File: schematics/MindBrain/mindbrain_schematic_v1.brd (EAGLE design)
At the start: 100 x 80 mm, 47 parts, among them CON1 POWER, IC1 TL084P, IC2 TL084P

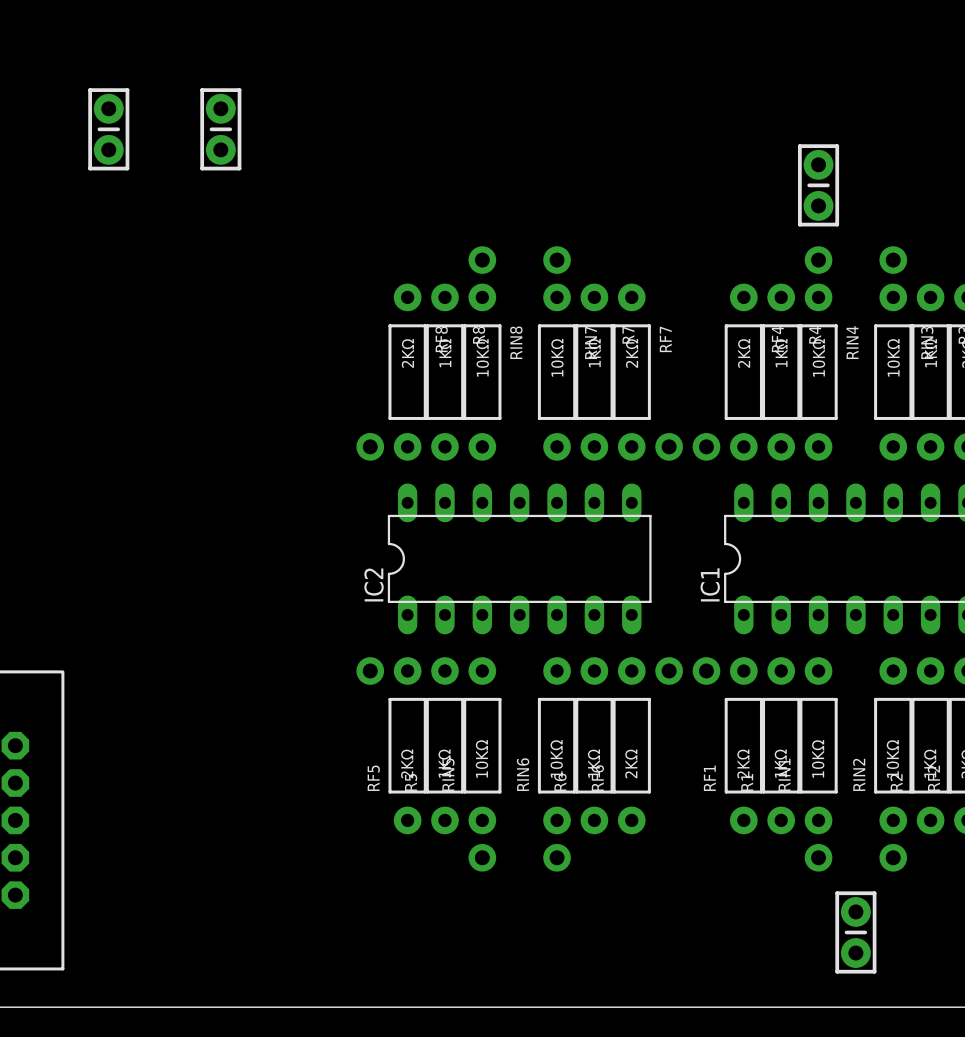
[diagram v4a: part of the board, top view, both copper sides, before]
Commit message: placed bypass caps in board view
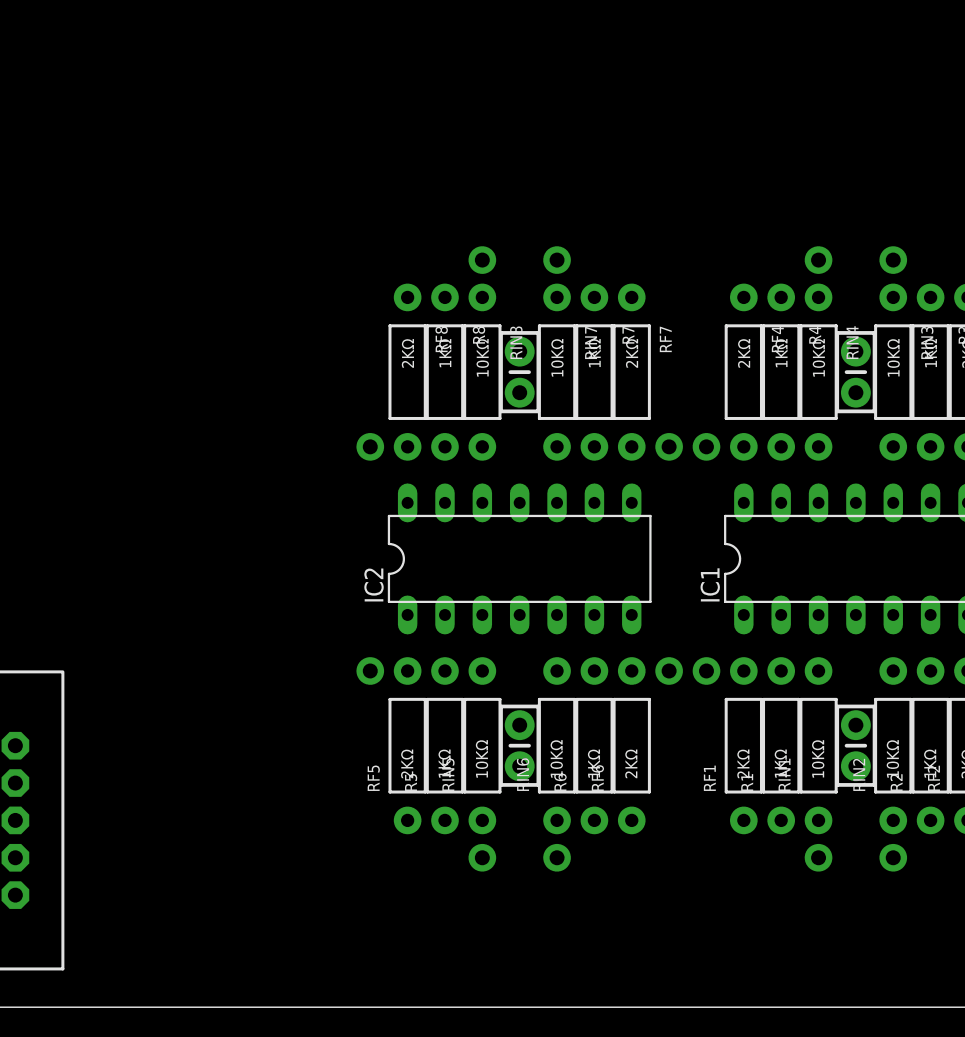
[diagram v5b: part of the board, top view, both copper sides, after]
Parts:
- moved C1 50.4 mm to (41.9, 17.8), turned to 270 degrees
- moved C3 38.2 mm to (64.8, 17.8), turned to 270 degrees
- moved C2 38.1 mm to (64.8, 43.2)
- moved C4 26.2 mm to (41.9, 43.2)
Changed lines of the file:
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@@
 <element name="RIN7" library="SparkFun-Passives" package="AXIAL-0.4" value="10KΩ" x="44.45" y="43.18" rot="R270"/>
 <element name="RIN8" library="SparkFun-Passives" package="AXIAL-0.4" value="10KΩ" x="39.37" y="43.18" rot="R270"/>
-<element name="C1" library="SparkFun-Capacitors" package="CAP-PTH-SMALL-KIT" value="0.1uF" x="13.97" y="59.69" rot="R90"/>
-<element name="C2" library="SparkFun-Capacitors" package="CAP-PTH-SMALL-KIT" value="0.1uF" x="64.77" y="5.08" rot="R90"/>
-<element name="C3" library="SparkFun-Capacitors" package="CAP-PTH-SMALL-KIT" value="0.1uF" x="62.23" y="55.88" rot="R90"/>
-<element name="C4" library="SparkFun-Capacitors" package="CAP-PTH-SMALL-KIT" value="0.1uF" x="21.59" y="59.69" rot="R90"/>
+<element name="C1" library="SparkFun-Capacitors" package="CAP-PTH-SMALL-KIT" value="0.1uF" x="41.91" y="17.78" rot="R270"/>
+<element name="C2" library="SparkFun-Capacitors" package="CAP-PTH-SMALL-KIT" value="0.1uF" x="64.77" y="43.18" rot="R90"/>
+<element name="C3" library="SparkFun-Capacitors" package="CAP-PTH-SMALL-KIT" value="0.1uF" x="64.77" y="17.78" rot="R270"/>
+<element name="C4" library="SparkFun-Capacitors" package="CAP-PTH-SMALL-KIT" value="0.1uF" x="41.91" y="43.18" rot="R90"/>
 <element name="CON1" library="SparkFun-Connectors" package="2X5-SHROUDED" value="POWER" x="6.35" y="12.7"/>
 </elements>
@@
 <wire x1="62.23" y1="48.26" x2="67.31" y2="48.26" width="0" layer="19" extent="1-1"/>
 <wire x1="59.69" y1="48.26" x2="62.23" y2="48.26" width="0" layer="19" extent="1-1"/>
-<wire x1="62.23" y1="57.277" x2="62.23" y2="48.26" width="0" layer="19" extent="1-1"/>
+<wire x1="64.77" y1="16.383" x2="62.23" y2="48.26" width="0" layer="19" extent="1-1"/>
 <wire x1="46.99" y1="48.26" x2="59.69" y2="48.26" width="0" layer="19" extent="1-1"/>
 <wire x1="44.45" y1="48.26" x2="46.99" y2="48.26" width="0" layer="19" extent="1-1"/>
 <wire x1="39.37" y1="48.26" x2="44.45" y2="48.26" width="0" layer="19" extent="1-1"/>
 <wire x1="36.83" y1="48.26" x2="39.37" y2="48.26" width="0" layer="19" extent="1-1"/>
-<wire x1="21.59" y1="61.087" x2="36.83" y2="48.26" width="0" layer="19" extent="1-1"/>
-<wire x1="13.97" y1="61.087" x2="21.59" y2="61.087" width="0" layer="19" extent="1-1"/>
+<wire x1="41.91" y1="44.577" x2="36.83" y2="48.26" width="0" layer="19" extent="1-1"/>
+<wire x1="41.91" y1="16.383" x2="41.91" y2="44.577" width="0" layer="19" extent="1-1"/>
 <wire x1="69.85" y1="12.7" x2="69.85" y2="48.26" width="0" layer="19" extent="1-1"/>
 <wire x1="67.31" y1="12.7" x2="69.85" y2="12.7" width="0" layer="19" extent="1-1"/>
 <wire x1="62.23" y1="12.7" x2="67.31" y2="12.7" width="0" layer="19" extent="1-1"/>
 <wire x1="59.69" y1="12.7" x2="62.23" y2="12.7" width="0" layer="19" extent="1-1"/>
-<wire x1="64.77" y1="6.477" x2="67.31" y2="12.7" width="0" layer="19" extent="1-1"/>
+<wire x1="64.77" y1="44.577" x2="67.31" y2="12.7" width="0" layer="19" extent="1-1"/>
 <wire x1="46.99" y1="12.7" x2="59.69" y2="12.7" width="0" layer="19" extent="1-1"/>
 <wire x1="44.45" y1="12.7" x2="46.99" y2="12.7" width="0" layer="19" extent="1-1"/>
@@
 <contactref element="C4" pad="1"/>
 <wire x1="41.91" y1="34.29" x2="64.77" y2="34.29" width="0" layer="19" extent="1-1"/>
-<wire x1="64.77" y1="3.683" x2="64.77" y2="34.29" width="0" layer="19" extent="1-1"/>
-<wire x1="21.59" y1="58.293" x2="41.91" y2="34.29" width="0" layer="19" extent="1-1"/>
+<wire x1="64.77" y1="41.783" x2="64.77" y2="34.29" width="0" layer="19" extent="1-1"/>
+<wire x1="41.91" y1="41.783" x2="41.91" y2="34.29" width="0" layer="19" extent="1-1"/>
 <wire x1="7.62" y1="17.78" x2="41.91" y2="34.29" width="0" layer="19" extent="1-1"/>
 <wire x1="5.08" y1="17.78" x2="7.62" y2="17.78" width="0" layer="19" extent="1-1"/>
@@
 <contactref element="C3" pad="1"/>
 <contactref element="CON1" pad="10"/>
-<wire x1="64.77" y1="26.67" x2="62.23" y2="54.483" width="0" layer="19" extent="1-1"/>
+<wire x1="64.77" y1="26.67" x2="64.77" y2="19.177" width="0" layer="19" extent="1-1"/>
 <wire x1="41.91" y1="26.67" x2="64.77" y2="26.67" width="0" layer="19" extent="1-1"/>
 <wire x1="7.62" y1="7.62" x2="41.91" y2="26.67" width="0" layer="19" extent="1-1"/>
 <wire x1="5.08" y1="7.62" x2="7.62" y2="7.62" width="0" layer="19" extent="1-1"/>
-<wire x1="13.97" y1="58.293" x2="41.91" y2="26.67" width="0" layer="19" extent="1-1"/>
+<wire x1="41.91" y1="19.177" x2="41.91" y2="26.67" width="0" layer="19" extent="1-1"/>
 </signal>
 </signals>

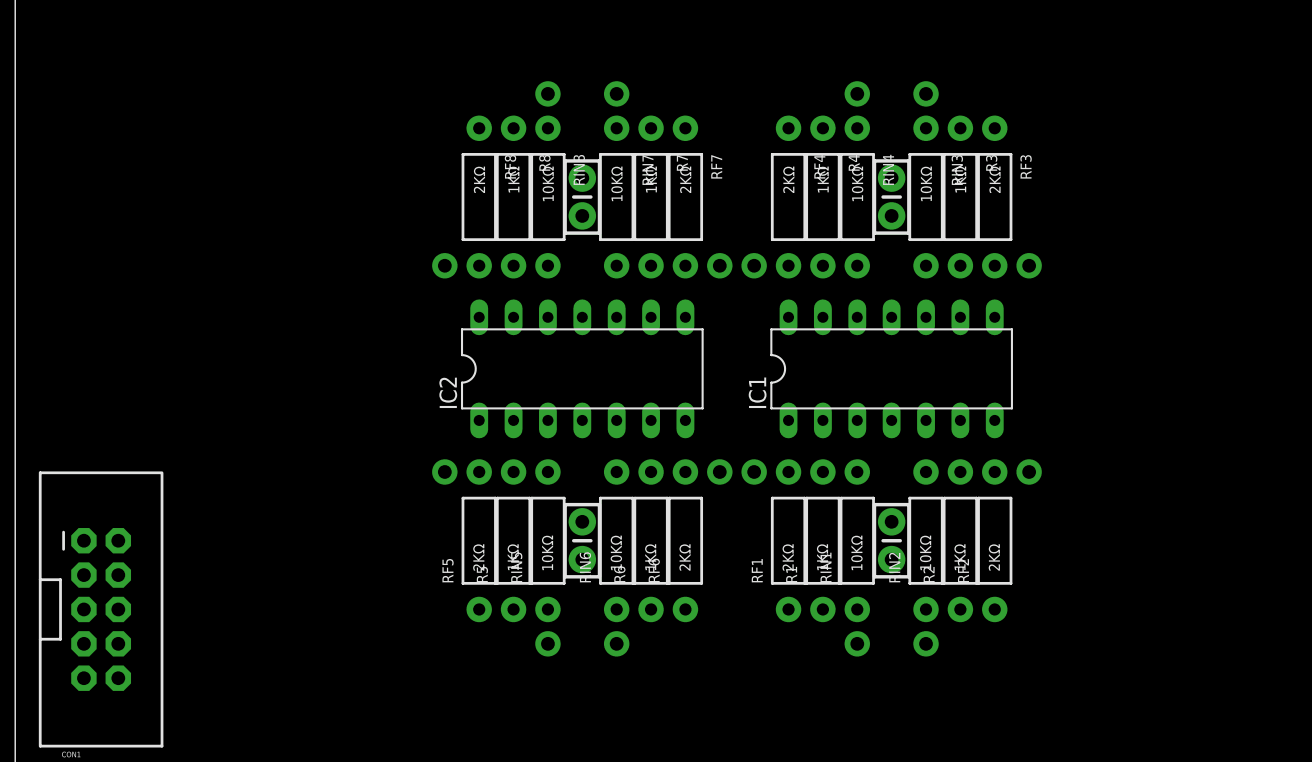
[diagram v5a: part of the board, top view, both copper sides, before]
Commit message: started laying traces, top side
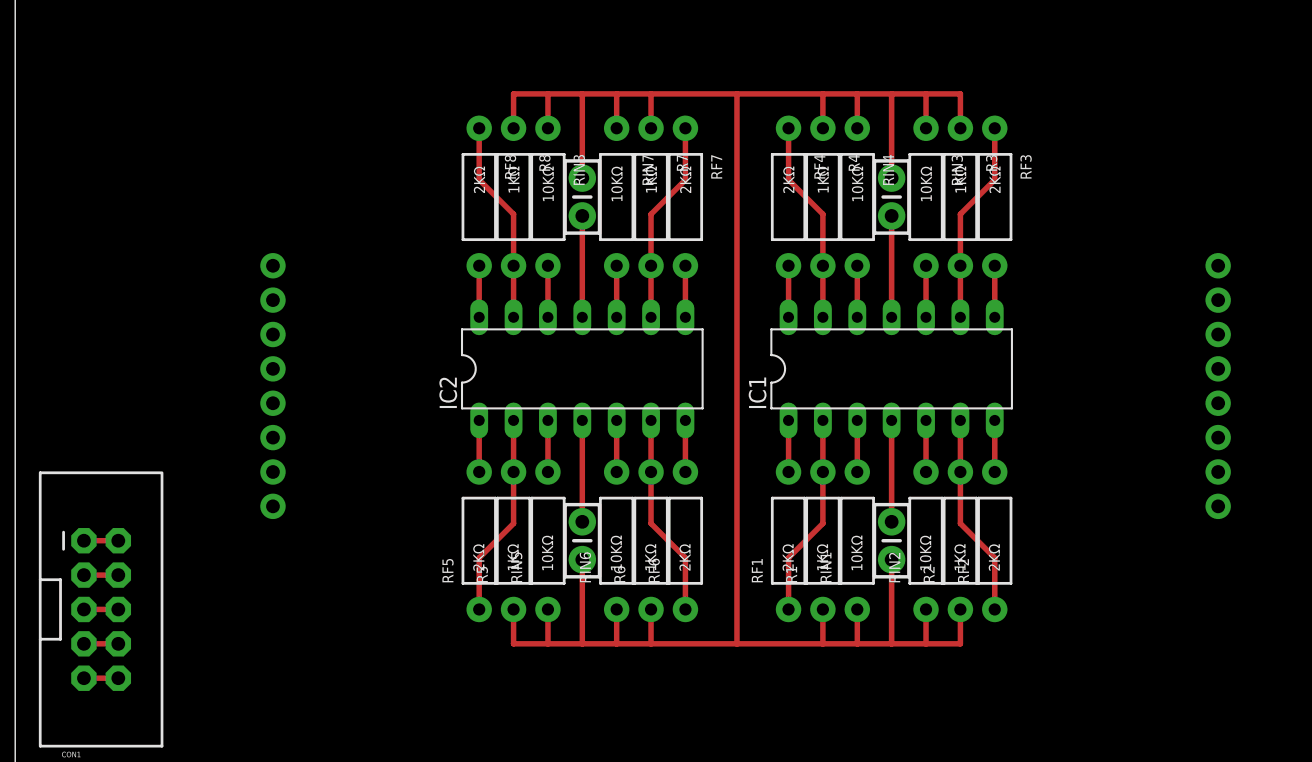
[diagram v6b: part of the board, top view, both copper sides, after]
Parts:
- moved OUTPUT5 57.7 mm to (88.9, 30.5)
- moved OUTPUT8 57.2 mm to (88.9, 38.1)
- moved INPUT3 54.5 mm to (19.1, 25.4)
- moved INPUT2 49.9 mm to (19.1, 22.9)
- moved INPUT4 48.9 mm to (19.1, 27.9)
- moved INPUT1 44.4 mm to (19.1, 20.3)
- moved OUTPUT6 38.2 mm to (88.9, 33.0)
- moved OUTPUT7 36.9 mm to (88.9, 35.6)
- moved OUTPUT4 35.8 mm to (88.9, 27.9)
- moved OUTPUT1 34.4 mm to (88.9, 20.3)
- moved INPUT6 34.2 mm to (19.1, 33.0)
- moved INPUT7 29.6 mm to (19.1, 35.6)
- moved INPUT5 28.7 mm to (19.1, 30.5)
- moved INPUT8 24.0 mm to (19.1, 38.1)
- moved OUTPUT3 18.9 mm to (88.9, 25.4)
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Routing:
- net GND: track 0.00 -> 179.8 mm
- net N$27: track 0.00 -> 17.5 mm
- net N$25: track 0.00 -> 17.5 mm
- net N$6: track 0.00 -> 15.0 mm
- net N$9: track 0.00 -> 15.0 mm
- net N$3: track 0.00 -> 15.0 mm
- net N$18: track 0.00 -> 15.0 mm
- net N$15: track 0.00 -> 15.0 mm
- net N$24: track 0.00 -> 15.0 mm
- net N$21: track 0.00 -> 15.0 mm
- net N$12: track 0.00 -> 15.0 mm
- net N$8: track 0.00 -> 3.81 mm
- net N$7: track 0.00 -> 3.81 mm
- net N$5: track 0.00 -> 3.81 mm
- net N$4: track 0.00 -> 3.81 mm
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
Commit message: updated top layer layouts
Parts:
- moved CON1 16.6 mm to (7.62, 29.2)
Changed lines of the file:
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@@
 <element name="C3" library="SparkFun-Capacitors" package="CAP-PTH-SMALL-KIT" value="0.1uF" x="64.77" y="17.78" rot="R270"/>
 <element name="C4" library="SparkFun-Capacitors" package="CAP-PTH-SMALL-KIT" value="0.1uF" x="41.91" y="43.18" rot="R90"/>
-<element name="CON1" library="SparkFun-Connectors" package="2X5-SHROUDED" value="POWER" x="6.35" y="12.7"/>
+<element name="CON1" library="SparkFun-Connectors" package="2X5-SHROUDED" value="POWER" x="7.62" y="29.21"/>
 </elements>
 <signals>
@@
 <contactref element="C1" pad="2"/>
 <contactref element="C3" pad="2"/>
-<wire x1="5.08" y1="10.16" x2="7.62" y2="10.16" width="0.4064" layer="1"/>
-<wire x1="5.08" y1="15.24" x2="7.62" y2="15.24" width="0.4064" layer="1"/>
-<wire x1="5.08" y1="12.7" x2="7.62" y2="12.7" width="0.4064" layer="1"/>
+<wire x1="6.35" y1="26.67" x2="8.89" y2="26.67" width="0.4064" layer="1"/>
+<wire x1="6.35" y1="31.75" x2="8.89" y2="31.75" width="0.4064" layer="1"/>
+<wire x1="6.35" y1="29.21" x2="8.89" y2="29.21" width="0.4064" layer="1"/>
 <wire x1="39.37" y1="12.7" x2="39.37" y2="10.16" width="0.4064" layer="1"/>
 <wire x1="39.37" y1="10.16" x2="41.91" y2="10.16" width="0.4064" layer="1"/>
@@
 <wire x1="62.23" y1="10.16" x2="59.69" y2="10.16" width="0.4064" layer="1"/>
 <wire x1="53.34" y1="10.16" x2="53.34" y2="50.8" width="0.4064" layer="1"/>
-<wire x1="7.62" y1="12.7" x2="36.83" y2="12.7" width="0" layer="19" extent="1-1"/>
-<wire x1="7.62" y1="15.24" x2="7.62" y2="12.7" width="0" layer="19" extent="1-1"/>
-<wire x1="7.62" y1="10.16" x2="7.62" y2="12.7" width="0" layer="19" extent="1-1"/>
+<wire x1="8.89" y1="29.21" x2="36.83" y2="12.7" width="0" layer="19" extent="1-1"/>
+<wire x1="8.89" y1="31.75" x2="8.89" y2="29.21" width="0" layer="19" extent="1-1"/>
+<wire x1="8.89" y1="26.67" x2="8.89" y2="29.21" width="0" layer="19" extent="1-1"/>
 </signal>
 <signal name="N$2">
@@
 <wire x1="64.77" y1="41.783" x2="64.77" y2="34.29" width="0.4064" layer="1"/>
 <wire x1="41.91" y1="41.783" x2="41.91" y2="34.29" width="0.4064" layer="1"/>
-<wire x1="7.62" y1="17.78" x2="41.91" y2="34.29" width="0" layer="19" extent="1-1"/>
-<wire x1="5.08" y1="17.78" x2="7.62" y2="17.78" width="0.4064" layer="1"/>
+<wire x1="8.89" y1="34.29" x2="41.91" y2="34.29" width="0" layer="19" extent="1-1"/>
+<wire x1="6.35" y1="34.29" x2="8.89" y2="34.29" width="0.4064" layer="1"/>
 </signal>
 <signal name="N$25">
@@
 <contactref element="CON1" pad="10"/>
 <wire x1="41.91" y1="26.67" x2="64.77" y2="26.67" width="0" layer="19" extent="1-1"/>
-<wire x1="7.62" y1="7.62" x2="41.91" y2="26.67" width="0" layer="19" extent="1-1"/>
+<wire x1="8.89" y1="24.13" x2="41.91" y2="26.67" width="0" layer="19" extent="1-1"/>
 <wire x1="64.77" y1="19.177" x2="64.77" y2="26.67" width="0.4064" layer="1"/>
 <wire x1="41.91" y1="19.177" x2="41.91" y2="26.67" width="0.4064" layer="1"/>
-<wire x1="5.08" y1="7.62" x2="7.62" y2="7.62" width="0.4064" layer="1"/>
+<wire x1="6.35" y1="24.13" x2="8.89" y2="24.13" width="0.4064" layer="1"/>
 </signal>
 </signals>

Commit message: replaced ground traces with ground pour
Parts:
- moved C1 5.08 mm to (41.9, 12.7)
- moved C3 5.08 mm to (64.8, 12.7)
- moved CON1 5.08 mm to (7.62, 24.1)
- moved IC1 5.08 mm to (64.8, 25.4)
- moved IC2 5.08 mm to (41.9, 25.4)
- moved INPUT4 5.08 mm to (19.1, 22.9)
- moved INPUT5 5.08 mm to (19.1, 25.4)
- moved INPUT6 5.08 mm to (19.1, 27.9)
- moved INPUT7 5.08 mm to (19.1, 30.5)
- moved OUTPUT4 5.08 mm to (88.9, 22.9)
- moved OUTPUT5 5.08 mm to (88.9, 25.4)
- moved OUTPUT6 5.08 mm to (88.9, 27.9)
- moved OUTPUT7 5.08 mm to (88.9, 30.5)
- moved R1 5.08 mm to (59.7, 12.7)
- moved R2 5.08 mm to (69.8, 12.7)
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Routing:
- net GND: track 179.8 -> 7.62 mm
- added copper zone on layer 1, net GND
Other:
- board size 100 x 80 mm -> 92.4 x 49.5 mm
